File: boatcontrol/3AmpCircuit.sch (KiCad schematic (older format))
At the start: 5 parts, among them K1 G5RL-K1A-E-DC12, Q2 T9-818 3A, SW1 ESB30, SW2 ESB30

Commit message: Before starting the PCB fresh
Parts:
- renumbered D3 to D401, K1 to K401, Q2 to Q401, SW1 to SW401, SW2 to SW402

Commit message: Structured
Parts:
- Q401: footprint BoatControl:SchurterCurcuitBreaker -> BoatControl:Schurter_Circuit_Breaker
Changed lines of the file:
@@
 $Descr A4 11693 8268
 encoding utf-8
-Sheet 4 55
+Sheet 19 55
 Title "Boat Control Hat"
 Date "2020-07-09"
@@
 AR Path="/D16552B4/5FA17F6C/D2B5CDA5/E14E2027" Ref="D1601"  Part="1"
 AR Path="/D16552B4/5FA17F6C/D2F3142B/E14E2027" Ref="D1701"  Part="1"
-F 0 "D401" H 5900 3850 50  0000 C CNN
+F 0 "D1901" H 5900 3850 50  0000 C CNN
 F 1 "WP115VGYW" H 6050 3750 50  0000 C CNN
 F 2 "LED_THT:LED_D5.0mm-3" H 6100 4000 50  0001 C CNN
@@
 AR Path="/D16552B4/5FA17F6C/D2B5CDA5/D2F4D9A8" Ref="K1601"  Part="1"
 AR Path="/D16552B4/5FA17F6C/D2F3142B/D2F4D9A8" Ref="K1701"  Part="1"
-F 0 "K401" H 7250 4000 50  0000 L CNN
+F 0 "K1901" H 7250 4000 50  0000 L CNN
 F 1 "G5RL-K1A-E-DC12" H 7600 4000 50  0000 L CNN
 F 2 "RELAY_G5RL-K1A-E-DC12" H 7600 4150 50  0001 L BNN
@@
 AR Path="/D16552B4/5FA17F6C/D2B5CDA5/6283485A" Ref="Q1601"  Part="1"
 AR Path="/D16552B4/5FA17F6C/D2F3142B/6283485A" Ref="Q1701"  Part="1"
-F 0 "Q401" V 7150 2950 50  0000 R CNN
+F 0 "Q1901" V 7150 2950 50  0000 R CNN
 F 1 "T9-818 3A" V 7150 2700 50  0000 R CNN
-F 2 "BoatControl:SchurterCurcuitBreaker" H 7150 3300 50  0001 C CNN
+F 2 "BoatControl:Schurter_Circuit_Breaker" H 7150 3300 50  0001 C CNN
 F 3 "https://eu.mouser.com/datasheet/2/358/typ_T9-818-1276014.pdf" H 7150 3300 50  0001 C CNN
 F 4 "4404.0096" V 7150 3300 50  0001 C CNN "Manufacturer ID"
@@
 AR Path="/D16552B4/5FA17F6C/D2B5CDA5/63E25899" Ref="SW1601"  Part="1"
 AR Path="/D16552B4/5FA17F6C/D2F3142B/63E25899" Ref="SW1701"  Part="1"
-F 0 "SW401" V 6050 3900 50  0000 C CNN
+F 0 "SW1901" V 6050 3900 50  0000 C CNN
 F 1 " ESB30" V 6000 3400 50  0000 C CNN
 F 2 "BoatControl:SW_PUSH_ESB30_DPDT" H 6050 3550 50  0001 C CNN
@@
 AR Path="/D16552B4/5FA17F6C/D2B5CDA5/63ED7D79" Ref="#PWR01602"  Part="1"
 AR Path="/D16552B4/5FA17F6C/D2F3142B/63ED7D79" Ref="#PWR01702"  Part="1"
-F 0 "#PWR02202" H 6650 3750 50  0001 C CNN
+F 0 "#PWR01902" H 6650 3750 50  0001 C CNN
 F 1 "GND" H 6655 3827 50  0000 C CNN
 F 2 "" H 6650 4000 50  0001 C CNN
@@
 AR Path="/D16552B4/5FA17F6C/D2B5CDA5/D2B5CDA0" Ref="#PWR01601"  Part="1"
 AR Path="/D16552B4/5FA17F6C/D2F3142B/D2B5CDA0" Ref="#PWR01701"  Part="1"
-F 0 "#PWR02201" H 5250 3850 50  0001 C CNN
+F 0 "#PWR01901" H 5250 3850 50  0001 C CNN
 F 1 "+12P" H 5265 4173 50  0000 C CNN
 F 2 "" H 5250 4000 50  0001 C CNN
@@
 AR Path="/D16552B4/5FA17F6C/D2B5CDA5/D2B5CD9C" Ref="SW1602"  Part="1"
 AR Path="/D16552B4/5FA17F6C/D2F3142B/D2B5CD9C" Ref="SW1702"  Part="1"
-F 0 "SW402" V 6050 5250 50  0000 C CNN
+F 0 "SW1902" V 6050 5250 50  0000 C CNN
 F 1 " ESB30" V 6000 4700 50  0000 C CNN
 F 2 "BoatControl:SW_PUSH_ESB30_DPDT" H 6050 4900 50  0001 C CNN

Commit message: Organize more
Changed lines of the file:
@@
 AR Path="/D16552B4/5FA17F6C/D2B5CDA5/E14E2027" Ref="D1601"  Part="1"
 AR Path="/D16552B4/5FA17F6C/D2F3142B/E14E2027" Ref="D1701"  Part="1"
-F 0 "D1901" H 5900 3850 50  0000 C CNN
+F 0 "D2201" H 5900 3850 50  0000 C CNN
 F 1 "WP115VGYW" H 6050 3750 50  0000 C CNN
 F 2 "LED_THT:LED_D5.0mm-3" H 6100 4000 50  0001 C CNN
@@
 AR Path="/D16552B4/5FA17F6C/D2B5CDA5/D2F4D9A8" Ref="K1601"  Part="1"
 AR Path="/D16552B4/5FA17F6C/D2F3142B/D2F4D9A8" Ref="K1701"  Part="1"
-F 0 "K1901" H 7250 4000 50  0000 L CNN
+F 0 "K2201" H 7250 4000 50  0000 L CNN
 F 1 "G5RL-K1A-E-DC12" H 7600 4000 50  0000 L CNN
 F 2 "RELAY_G5RL-K1A-E-DC12" H 7600 4150 50  0001 L BNN
@@
 AR Path="/D16552B4/5FA17F6C/D2B5CDA5/6283485A" Ref="Q1601"  Part="1"
 AR Path="/D16552B4/5FA17F6C/D2F3142B/6283485A" Ref="Q1701"  Part="1"
-F 0 "Q1901" V 7150 2950 50  0000 R CNN
+F 0 "Q2201" V 7150 2950 50  0000 R CNN
 F 1 "T9-818 3A" V 7150 2700 50  0000 R CNN
 F 2 "BoatControl:Schurter_Circuit_Breaker" H 7150 3300 50  0001 C CNN
@@
 AR Path="/D16552B4/5FA17F6C/D2B5CDA5/63E25899" Ref="SW1601"  Part="1"
 AR Path="/D16552B4/5FA17F6C/D2F3142B/63E25899" Ref="SW1701"  Part="1"
-F 0 "SW1901" V 6050 3900 50  0000 C CNN
+F 0 "SW2201" V 6050 3900 50  0000 C CNN
 F 1 " ESB30" V 6000 3400 50  0000 C CNN
 F 2 "BoatControl:SW_PUSH_ESB30_DPDT" H 6050 3550 50  0001 C CNN
@@
 AR Path="/D16552B4/5FA17F6C/D2B5CDA5/63ED7D79" Ref="#PWR01602"  Part="1"
 AR Path="/D16552B4/5FA17F6C/D2F3142B/63ED7D79" Ref="#PWR01702"  Part="1"
-F 0 "#PWR01902" H 6650 3750 50  0001 C CNN
+F 0 "#PWR02202" H 6650 3750 50  0001 C CNN
 F 1 "GND" H 6655 3827 50  0000 C CNN
 F 2 "" H 6650 4000 50  0001 C CNN
@@
 AR Path="/D16552B4/5FA17F6C/D2B5CDA5/D2B5CDA0" Ref="#PWR01601"  Part="1"
 AR Path="/D16552B4/5FA17F6C/D2F3142B/D2B5CDA0" Ref="#PWR01701"  Part="1"
-F 0 "#PWR01901" H 5250 3850 50  0001 C CNN
+F 0 "#PWR02201" H 5250 3850 50  0001 C CNN
 F 1 "+12P" H 5265 4173 50  0000 C CNN
 F 2 "" H 5250 4000 50  0001 C CNN
@@
 AR Path="/D16552B4/5FA17F6C/D2B5CDA5/D2B5CD9C" Ref="SW1602"  Part="1"
 AR Path="/D16552B4/5FA17F6C/D2F3142B/D2B5CD9C" Ref="SW1702"  Part="1"
-F 0 "SW1902" V 6050 5250 50  0000 C CNN
+F 0 "SW2202" V 6050 5250 50  0000 C CNN
 F 1 " ESB30" V 6000 4700 50  0000 C CNN
 F 2 "BoatControl:SW_PUSH_ESB30_DPDT" H 6050 4900 50  0001 C CNN

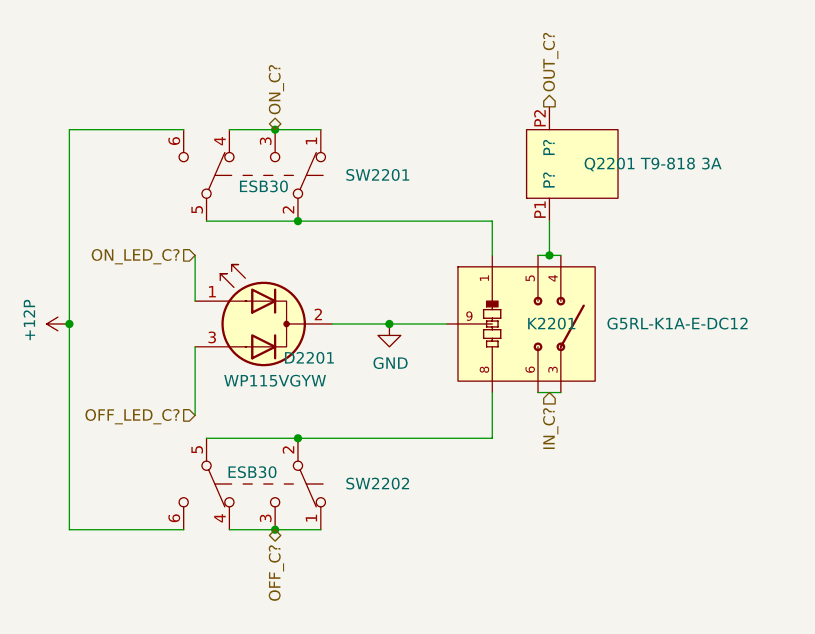
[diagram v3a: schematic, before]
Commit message: Start assigning net classes
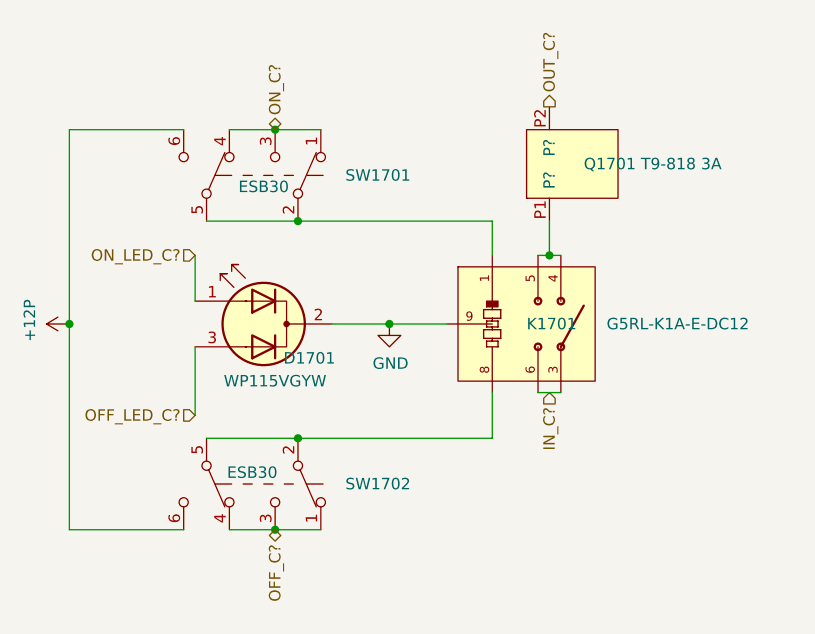
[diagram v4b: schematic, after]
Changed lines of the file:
@@
 $Descr A4 11693 8268
 encoding utf-8
-Sheet 19 55
+Sheet 17 55
 Title "Boat Control Hat"
 Date "2020-07-09"
@@
 AR Path="/D16552B4/5FA17F6C/D2B5CDA5/E14E2027" Ref="D1601"  Part="1"
 AR Path="/D16552B4/5FA17F6C/D2F3142B/E14E2027" Ref="D1701"  Part="1"
-F 0 "D2201" H 5900 3850 50  0000 C CNN
+F 0 "D1701" H 5900 3850 50  0000 C CNN
 F 1 "WP115VGYW" H 6050 3750 50  0000 C CNN
 F 2 "LED_THT:LED_D5.0mm-3" H 6100 4000 50  0001 C CNN
@@
 AR Path="/D16552B4/5FA17F6C/D2B5CDA5/D2F4D9A8" Ref="K1601"  Part="1"
 AR Path="/D16552B4/5FA17F6C/D2F3142B/D2F4D9A8" Ref="K1701"  Part="1"
-F 0 "K2201" H 7250 4000 50  0000 L CNN
+F 0 "K1701" H 7250 4000 50  0000 L CNN
 F 1 "G5RL-K1A-E-DC12" H 7600 4000 50  0000 L CNN
 F 2 "RELAY_G5RL-K1A-E-DC12" H 7600 4150 50  0001 L BNN
@@
 AR Path="/D16552B4/5FA17F6C/D2B5CDA5/6283485A" Ref="Q1601"  Part="1"
 AR Path="/D16552B4/5FA17F6C/D2F3142B/6283485A" Ref="Q1701"  Part="1"
-F 0 "Q2201" V 7150 2950 50  0000 R CNN
+F 0 "Q1701" V 7150 2950 50  0000 R CNN
 F 1 "T9-818 3A" V 7150 2700 50  0000 R CNN
 F 2 "BoatControl:Schurter_Circuit_Breaker" H 7150 3300 50  0001 C CNN
@@
 AR Path="/D16552B4/5FA17F6C/D2B5CDA5/63E25899" Ref="SW1601"  Part="1"
 AR Path="/D16552B4/5FA17F6C/D2F3142B/63E25899" Ref="SW1701"  Part="1"
-F 0 "SW2201" V 6050 3900 50  0000 C CNN
+F 0 "SW1701" V 6050 3900 50  0000 C CNN
 F 1 " ESB30" V 6000 3400 50  0000 C CNN
 F 2 "BoatControl:SW_PUSH_ESB30_DPDT" H 6050 3550 50  0001 C CNN
@@
 AR Path="/D16552B4/5FA17F6C/D2B5CDA5/63ED7D79" Ref="#PWR01602"  Part="1"
 AR Path="/D16552B4/5FA17F6C/D2F3142B/63ED7D79" Ref="#PWR01702"  Part="1"
-F 0 "#PWR02202" H 6650 3750 50  0001 C CNN
+F 0 "#PWR01702" H 6650 3750 50  0001 C CNN
 F 1 "GND" H 6655 3827 50  0000 C CNN
 F 2 "" H 6650 4000 50  0001 C CNN
@@
 AR Path="/D16552B4/5FA17F6C/D2B5CDA5/D2B5CDA0" Ref="#PWR01601"  Part="1"
 AR Path="/D16552B4/5FA17F6C/D2F3142B/D2B5CDA0" Ref="#PWR01701"  Part="1"
-F 0 "#PWR02201" H 5250 3850 50  0001 C CNN
+F 0 "#PWR01701" H 5250 3850 50  0001 C CNN
 F 1 "+12P" H 5265 4173 50  0000 C CNN
 F 2 "" H 5250 4000 50  0001 C CNN
@@
 AR Path="/D16552B4/5FA17F6C/D2B5CDA5/D2B5CD9C" Ref="SW1602"  Part="1"
 AR Path="/D16552B4/5FA17F6C/D2F3142B/D2B5CD9C" Ref="SW1702"  Part="1"
-F 0 "SW2202" V 6050 5250 50  0000 C CNN
+F 0 "SW1702" V 6050 5250 50  0000 C CNN
 F 1 " ESB30" V 6000 4700 50  0000 C CNN
 F 2 "BoatControl:SW_PUSH_ESB30_DPDT" H 6050 4900 50  0001 C CNN

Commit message: Before re-import
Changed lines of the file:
@@
 AR Path="/D16552B4/5FA17F6C/D2B5CDA5/E14E2027" Ref="D1601"  Part="1"
 AR Path="/D16552B4/5FA17F6C/D2F3142B/E14E2027" Ref="D1701"  Part="1"
-F 0 "D1701" H 5900 3850 50  0000 C CNN
+F 0 "D2201" H 5900 3850 50  0000 C CNN
 F 1 "WP115VGYW" H 6050 3750 50  0000 C CNN
 F 2 "LED_THT:LED_D5.0mm-3" H 6100 4000 50  0001 C CNN
@@
 AR Path="/D16552B4/5FA17F6C/D2B5CDA5/D2F4D9A8" Ref="K1601"  Part="1"
 AR Path="/D16552B4/5FA17F6C/D2F3142B/D2F4D9A8" Ref="K1701"  Part="1"
-F 0 "K1701" H 7250 4000 50  0000 L CNN
+F 0 "K2201" H 7250 4000 50  0000 L CNN
 F 1 "G5RL-K1A-E-DC12" H 7600 4000 50  0000 L CNN
 F 2 "RELAY_G5RL-K1A-E-DC12" H 7600 4150 50  0001 L BNN
@@
 AR Path="/D16552B4/5FA17F6C/D2B5CDA5/6283485A" Ref="Q1601"  Part="1"
 AR Path="/D16552B4/5FA17F6C/D2F3142B/6283485A" Ref="Q1701"  Part="1"
-F 0 "Q1701" V 7150 2950 50  0000 R CNN
+F 0 "Q2201" V 7150 2950 50  0000 R CNN
 F 1 "T9-818 3A" V 7150 2700 50  0000 R CNN
 F 2 "BoatControl:Schurter_Circuit_Breaker" H 7150 3300 50  0001 C CNN
@@
 AR Path="/D16552B4/5FA17F6C/D2B5CDA5/63E25899" Ref="SW1601"  Part="1"
 AR Path="/D16552B4/5FA17F6C/D2F3142B/63E25899" Ref="SW1701"  Part="1"
-F 0 "SW1701" V 6050 3900 50  0000 C CNN
+F 0 "SW2201" V 6050 3900 50  0000 C CNN
 F 1 " ESB30" V 6000 3400 50  0000 C CNN
 F 2 "BoatControl:SW_PUSH_ESB30_DPDT" H 6050 3550 50  0001 C CNN
@@
 AR Path="/D16552B4/5FA17F6C/D2B5CDA5/63ED7D79" Ref="#PWR01602"  Part="1"
 AR Path="/D16552B4/5FA17F6C/D2F3142B/63ED7D79" Ref="#PWR01702"  Part="1"
-F 0 "#PWR01702" H 6650 3750 50  0001 C CNN
+F 0 "#PWR02202" H 6650 3750 50  0001 C CNN
 F 1 "GND" H 6655 3827 50  0000 C CNN
 F 2 "" H 6650 4000 50  0001 C CNN
@@
 AR Path="/D16552B4/5FA17F6C/D2B5CDA5/D2B5CDA0" Ref="#PWR01601"  Part="1"
 AR Path="/D16552B4/5FA17F6C/D2F3142B/D2B5CDA0" Ref="#PWR01701"  Part="1"
-F 0 "#PWR01701" H 5250 3850 50  0001 C CNN
+F 0 "#PWR02201" H 5250 3850 50  0001 C CNN
 F 1 "+12P" H 5265 4173 50  0000 C CNN
 F 2 "" H 5250 4000 50  0001 C CNN
@@
 AR Path="/D16552B4/5FA17F6C/D2B5CDA5/D2B5CD9C" Ref="SW1602"  Part="1"
 AR Path="/D16552B4/5FA17F6C/D2F3142B/D2B5CD9C" Ref="SW1702"  Part="1"
-F 0 "SW1702" V 6050 5250 50  0000 C CNN
+F 0 "SW2202" V 6050 5250 50  0000 C CNN
 F 1 " ESB30" V 6000 4700 50  0000 C CNN
 F 2 "BoatControl:SW_PUSH_ESB30_DPDT" H 6050 4900 50  0001 C CNN

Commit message: Before pull-up
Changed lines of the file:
@@
 $Descr A4 11693 8268
 encoding utf-8
-Sheet 17 55
+Sheet 5 59
 Title "Boat Control Hat"
 Date "2020-07-09"
@@
 AR Path="/D16552B4/5FA17F6C/D2B5CDA5/E14E2027" Ref="D1601"  Part="1"
 AR Path="/D16552B4/5FA17F6C/D2F3142B/E14E2027" Ref="D1701"  Part="1"
-F 0 "D2201" H 5900 3850 50  0000 C CNN
+F 0 "D501" H 5900 3850 50  0000 C CNN
 F 1 "WP115VGYW" H 6050 3750 50  0000 C CNN
 F 2 "LED_THT:LED_D5.0mm-3" H 6100 4000 50  0001 C CNN
@@
 AR Path="/D16552B4/5FA17F6C/D2B5CDA5/D2F4D9A8" Ref="K1601"  Part="1"
 AR Path="/D16552B4/5FA17F6C/D2F3142B/D2F4D9A8" Ref="K1701"  Part="1"
-F 0 "K2201" H 7250 4000 50  0000 L CNN
+F 0 "K501" H 7250 4000 50  0000 L CNN
 F 1 "G5RL-K1A-E-DC12" H 7600 4000 50  0000 L CNN
 F 2 "RELAY_G5RL-K1A-E-DC12" H 7600 4150 50  0001 L BNN
@@
 AR Path="/D16552B4/5FA17F6C/D2B5CDA5/6283485A" Ref="Q1601"  Part="1"
 AR Path="/D16552B4/5FA17F6C/D2F3142B/6283485A" Ref="Q1701"  Part="1"
-F 0 "Q2201" V 7150 2950 50  0000 R CNN
+F 0 "Q501" V 7150 2950 50  0000 R CNN
 F 1 "T9-818 3A" V 7150 2700 50  0000 R CNN
 F 2 "BoatControl:Schurter_Circuit_Breaker" H 7150 3300 50  0001 C CNN
@@
 AR Path="/D16552B4/5FA17F6C/D2B5CDA5/63E25899" Ref="SW1601"  Part="1"
 AR Path="/D16552B4/5FA17F6C/D2F3142B/63E25899" Ref="SW1701"  Part="1"
-F 0 "SW2201" V 6050 3900 50  0000 C CNN
+F 0 "SW501" V 6050 3900 50  0000 C CNN
 F 1 " ESB30" V 6000 3400 50  0000 C CNN
 F 2 "BoatControl:SW_PUSH_ESB30_DPDT" H 6050 3550 50  0001 C CNN
@@
 AR Path="/D16552B4/5FA17F6C/D2B5CDA5/63ED7D79" Ref="#PWR01602"  Part="1"
 AR Path="/D16552B4/5FA17F6C/D2F3142B/63ED7D79" Ref="#PWR01702"  Part="1"
-F 0 "#PWR02202" H 6650 3750 50  0001 C CNN
+F 0 "#PWR0502" H 6650 3750 50  0001 C CNN
 F 1 "GND" H 6655 3827 50  0000 C CNN
 F 2 "" H 6650 4000 50  0001 C CNN
@@
 AR Path="/D16552B4/5FA17F6C/D2B5CDA5/D2B5CDA0" Ref="#PWR01601"  Part="1"
 AR Path="/D16552B4/5FA17F6C/D2F3142B/D2B5CDA0" Ref="#PWR01701"  Part="1"
-F 0 "#PWR02201" H 5250 3850 50  0001 C CNN
+F 0 "#PWR0501" H 5250 3850 50  0001 C CNN
 F 1 "+12P" H 5265 4173 50  0000 C CNN
 F 2 "" H 5250 4000 50  0001 C CNN
@@
 AR Path="/D16552B4/5FA17F6C/D2B5CDA5/D2B5CD9C" Ref="SW1602"  Part="1"
 AR Path="/D16552B4/5FA17F6C/D2F3142B/D2B5CD9C" Ref="SW1702"  Part="1"
-F 0 "SW2202" V 6050 5250 50  0000 C CNN
+F 0 "SW502" V 6050 5250 50  0000 C CNN
 F 1 " ESB30" V 6000 4700 50  0000 C CNN
 F 2 "BoatControl:SW_PUSH_ESB30_DPDT" H 6050 4900 50  0001 C CNN

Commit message: Restructure
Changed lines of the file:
@@
 $Descr A4 11693 8268
 encoding utf-8
-Sheet 5 59
+Sheet 10 71
 Title "Boat Control Hat"
 Date "2020-07-09"
@@
 AR Path="/D16552B4/5FA17F6C/D2B5CDA5/E14E2027" Ref="D1601"  Part="1"
 AR Path="/D16552B4/5FA17F6C/D2F3142B/E14E2027" Ref="D1701"  Part="1"
-F 0 "D501" H 5900 3850 50  0000 C CNN
+F 0 "D901" H 5900 3850 50  0000 C CNN
 F 1 "WP115VGYW" H 6050 3750 50  0000 C CNN
 F 2 "LED_THT:LED_D5.0mm-3" H 6100 4000 50  0001 C CNN
@@
 AR Path="/D16552B4/5FA17F6C/D2B5CDA5/D2F4D9A8" Ref="K1601"  Part="1"
 AR Path="/D16552B4/5FA17F6C/D2F3142B/D2F4D9A8" Ref="K1701"  Part="1"
-F 0 "K501" H 7250 4000 50  0000 L CNN
+F 0 "K901" H 7250 4000 50  0000 L CNN
 F 1 "G5RL-K1A-E-DC12" H 7600 4000 50  0000 L CNN
 F 2 "RELAY_G5RL-K1A-E-DC12" H 7600 4150 50  0001 L BNN
@@
 AR Path="/D16552B4/5FA17F6C/D2B5CDA5/6283485A" Ref="Q1601"  Part="1"
 AR Path="/D16552B4/5FA17F6C/D2F3142B/6283485A" Ref="Q1701"  Part="1"
-F 0 "Q501" V 7150 2950 50  0000 R CNN
+F 0 "Q901" V 7150 2950 50  0000 R CNN
 F 1 "T9-818 3A" V 7150 2700 50  0000 R CNN
 F 2 "BoatControl:Schurter_Circuit_Breaker" H 7150 3300 50  0001 C CNN
@@
 AR Path="/D16552B4/5FA17F6C/D2B5CDA5/63E25899" Ref="SW1601"  Part="1"
 AR Path="/D16552B4/5FA17F6C/D2F3142B/63E25899" Ref="SW1701"  Part="1"
-F 0 "SW501" V 6050 3900 50  0000 C CNN
+F 0 "SW901" V 6050 3900 50  0000 C CNN
 F 1 " ESB30" V 6000 3400 50  0000 C CNN
 F 2 "BoatControl:SW_PUSH_ESB30_DPDT" H 6050 3550 50  0001 C CNN
@@
 AR Path="/D16552B4/5FA17F6C/D2B5CDA5/63ED7D79" Ref="#PWR01602"  Part="1"
 AR Path="/D16552B4/5FA17F6C/D2F3142B/63ED7D79" Ref="#PWR01702"  Part="1"
-F 0 "#PWR0502" H 6650 3750 50  0001 C CNN
+F 0 "#PWR0902" H 6650 3750 50  0001 C CNN
 F 1 "GND" H 6655 3827 50  0000 C CNN
 F 2 "" H 6650 4000 50  0001 C CNN
@@
 AR Path="/D16552B4/5FA17F6C/D2B5CDA5/D2B5CDA0" Ref="#PWR01601"  Part="1"
 AR Path="/D16552B4/5FA17F6C/D2F3142B/D2B5CDA0" Ref="#PWR01701"  Part="1"
-F 0 "#PWR0501" H 5250 3850 50  0001 C CNN
+F 0 "#PWR0901" H 5250 3850 50  0001 C CNN
 F 1 "+12P" H 5265 4173 50  0000 C CNN
 F 2 "" H 5250 4000 50  0001 C CNN
@@
 AR Path="/D16552B4/5FA17F6C/D2B5CDA5/D2B5CD9C" Ref="SW1602"  Part="1"
 AR Path="/D16552B4/5FA17F6C/D2F3142B/D2B5CD9C" Ref="SW1702"  Part="1"
-F 0 "SW502" V 6050 5250 50  0000 C CNN
+F 0 "SW902" V 6050 5250 50  0000 C CNN
 F 1 " ESB30" V 6000 4700 50  0000 C CNN
 F 2 "BoatControl:SW_PUSH_ESB30_DPDT" H 6050 4900 50  0001 C CNN

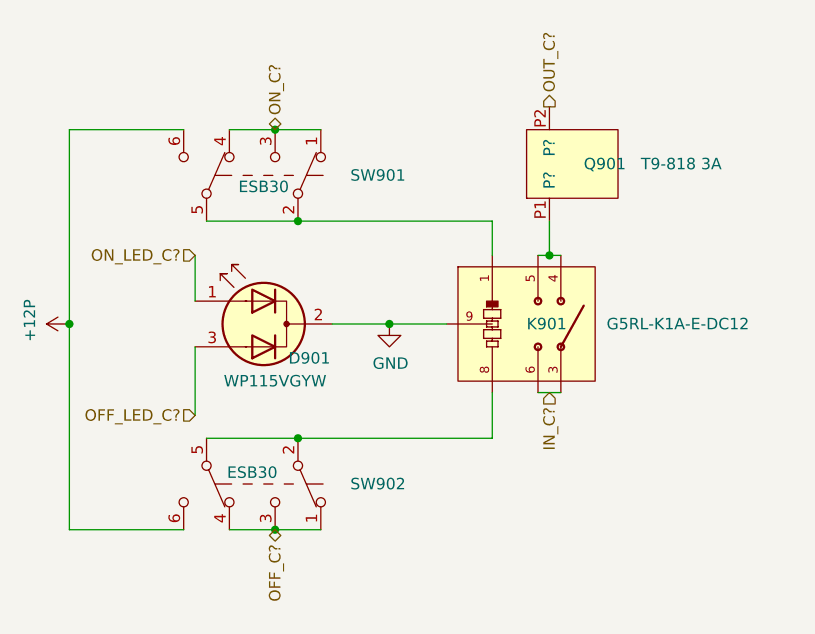
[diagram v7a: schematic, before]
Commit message: logig to dig name change
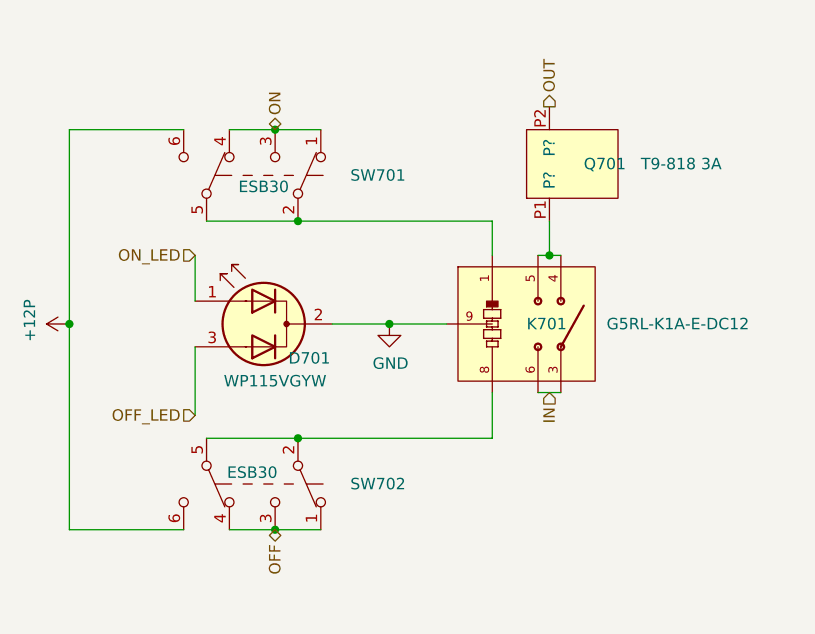
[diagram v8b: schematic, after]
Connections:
- net IN_C? renamed IN
- net OFF_C? renamed OFF
- net OFF_LED_C? renamed OFF_LED
- net ON_C? renamed ON
- net ON_LED_C? renamed ON_LED
- net OUT_C? renamed OUT
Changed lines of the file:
@@
 $Descr A4 11693 8268
 encoding utf-8
-Sheet 10 71
+Sheet 7 71
 Title "Boat Control Hat"
 Date "2020-07-09"
@@
 AR Path="/D16552B4/5FA17F6C/D2B5CDA5/E14E2027" Ref="D1601"  Part="1"
 AR Path="/D16552B4/5FA17F6C/D2F3142B/E14E2027" Ref="D1701"  Part="1"
-F 0 "D901" H 5900 3850 50  0000 C CNN
+F 0 "D701" H 5900 3850 50  0000 C CNN
 F 1 "WP115VGYW" H 6050 3750 50  0000 C CNN
 F 2 "LED_THT:LED_D5.0mm-3" H 6100 4000 50  0001 C CNN
@@
 AR Path="/D16552B4/5FA17F6C/D2B5CDA5/D2F4D9A8" Ref="K1601"  Part="1"
 AR Path="/D16552B4/5FA17F6C/D2F3142B/D2F4D9A8" Ref="K1701"  Part="1"
-F 0 "K901" H 7250 4000 50  0000 L CNN
+F 0 "K701" H 7250 4000 50  0000 L CNN
 F 1 "G5RL-K1A-E-DC12" H 7600 4000 50  0000 L CNN
 F 2 "RELAY_G5RL-K1A-E-DC12" H 7600 4150 50  0001 L BNN
@@
 AR Path="/D16552B4/5FA17F6C/D2B5CDA5/6283485A" Ref="Q1601"  Part="1"
 AR Path="/D16552B4/5FA17F6C/D2F3142B/6283485A" Ref="Q1701"  Part="1"
-F 0 "Q901" V 7150 2950 50  0000 R CNN
+F 0 "Q701" V 7150 2950 50  0000 R CNN
 F 1 "T9-818 3A" V 7150 2700 50  0000 R CNN
 F 2 "BoatControl:Schurter_Circuit_Breaker" H 7150 3300 50  0001 C CNN
@@
 AR Path="/D16552B4/5FA17F6C/D2B5CDA5/63E25899" Ref="SW1601"  Part="1"
 AR Path="/D16552B4/5FA17F6C/D2F3142B/63E25899" Ref="SW1701"  Part="1"
-F 0 "SW901" V 6050 3900 50  0000 C CNN
+F 0 "SW701" V 6050 3900 50  0000 C CNN
 F 1 " ESB30" V 6000 3400 50  0000 C CNN
 F 2 "BoatControl:SW_PUSH_ESB30_DPDT" H 6050 3550 50  0001 C CNN
@@
 AR Path="/D16552B4/5FA17F6C/D2B5CDA5/63ED7D79" Ref="#PWR01602"  Part="1"
 AR Path="/D16552B4/5FA17F6C/D2F3142B/63ED7D79" Ref="#PWR01702"  Part="1"
-F 0 "#PWR0902" H 6650 3750 50  0001 C CNN
+F 0 "#PWR0702" H 6650 3750 50  0001 C CNN
 F 1 "GND" H 6655 3827 50  0000 C CNN
 F 2 "" H 6650 4000 50  0001 C CNN
@@
 AR Path="/D16552B4/5FA17F6C/D2B5CDA5/D2B5CDA0" Ref="#PWR01601"  Part="1"
 AR Path="/D16552B4/5FA17F6C/D2F3142B/D2B5CDA0" Ref="#PWR01701"  Part="1"
-F 0 "#PWR0901" H 5250 3850 50  0001 C CNN
+F 0 "#PWR0701" H 5250 3850 50  0001 C CNN
 F 1 "+12P" H 5265 4173 50  0000 C CNN
 F 2 "" H 5250 4000 50  0001 C CNN
@@
 AR Path="/D16552B4/5FA17F6C/D2B5CDA5/D2B5CD9C" Ref="SW1602"  Part="1"
 AR Path="/D16552B4/5FA17F6C/D2F3142B/D2B5CD9C" Ref="SW1702"  Part="1"
-F 0 "SW902" V 6050 5250 50  0000 C CNN
+F 0 "SW702" V 6050 5250 50  0000 C CNN
 F 1 " ESB30" V 6000 4700 50  0000 C CNN
 F 2 "BoatControl:SW_PUSH_ESB30_DPDT" H 6050 4900 50  0001 C CNN
@@
 	5850 3550 6250 3550
 Text HLabel 6150 3150 1    50   BiDi ~ 0
-ON_C?
+ON
 Text HLabel 6150 4900 3    50   BiDi ~ 0
-OFF_C?
+OFF
 Wire Wire Line
 	5250 4900 5750 4900
@@
 	5250 3150 5750 3150
 Text HLabel 5800 3700 0    50   Input ~ 0
-ON_LED_C?
+ON_LED
 Text HLabel 5800 4400 0    50   Input ~ 0
-OFF_LED_C?
+OFF_LED
 Wire Wire Line
 	5800 4100 5800 4400
@@
 Connection ~ 6250 4500
 Text HLabel 7350 3050 1    50   Output ~ 0
-OUT_C?
+OUT
 Text HLabel 7350 4300 3    50   Input ~ 0
-IN_C?
+IN
 Wire Wire Line
 	7400 4300 7300 4300
